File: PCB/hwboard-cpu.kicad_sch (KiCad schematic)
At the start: 2 parts, among them M1 CM0

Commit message: add sensors
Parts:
- removed JP1: ~{RPI_BOOT}, symbol Jumper:Jumper_2_Open
- removed M1: CM0, hwboard-bike-computer:CM0, symbol hwboard-bike-computer:CM0
- added U5: RASPBERRY_PI_ZERO_2_W, hwboard-bike-computer:MODULE_RASPBERRY_PI_ZERO_2_W, symbol hwboard-bike-computer:RASPBERRY_PI_ZERO_2_W
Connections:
- net 3V3_{OUT}: now also U5.1 (3V3_1), U5.17 (3V3_17)
- net 5V_{IN}: now also U5.2 (5V_2), U5.4 (5V_4)
- net GND: now also U5.14 (GND_14), U5.20 (GND_20), U5.25 (GND_25), U5.30 (GND_30), U5.34 (GND_34), U5.39 (GND_39), U5.6 (GND_6), U5.9 (GND_9)
- net I2C_{BUS}.SCL: now also U5.5 (GPIO3/SCL)
- net I2C_{BUS}.SDA: now also U5.3 (GPIO2/SDA1)
- new net SPI_{BUS}.MISO: U5.21 (GPIO9/SPI_MISO)
- new net SPI_{BUS}.MOSI: U5.19 (GPIO10/SPI_MOSI)
- new net SPI_{BUS}.SCLK: U5.23 (GPIO11/SPI_SCLK)
- new net SPI_{BUS}.~{CS}: U5.24 (GPIO8/SPI_~{CE0})
- new net UART_{BUS}.RX: U5.10 (GPIO15/RXD0)
- new net UART_{BUS}.TX: U5.8 (GPIO14/TXD0)
- no-connect marks 34 -> 0
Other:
- note added: "PinHeader 2x20 = 61304021121"

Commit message: Major change CPU and usage
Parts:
- removed U5: RASPBERRY_PI_ZERO_2_W, hwboard-bike-computer:MODULE_RASPBERRY_PI_ZERO_2_W, symbol hwboard-bike-computer:RASPBERRY_PI_ZERO_2_W
- added U5: STM32H743VITx, Package_QFP:LQFP-100_14x14mm_P0.5mm, symbol MCU_ST_STM32H7:STM32H743VITx
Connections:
- new net: U5.10 (VSS), U5.26 (VSS), U5.49 (VSS), U5.74 (VSS), U5.99 (VSS)
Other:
- note removed: "PinHeader 2x20 = 61304021121"

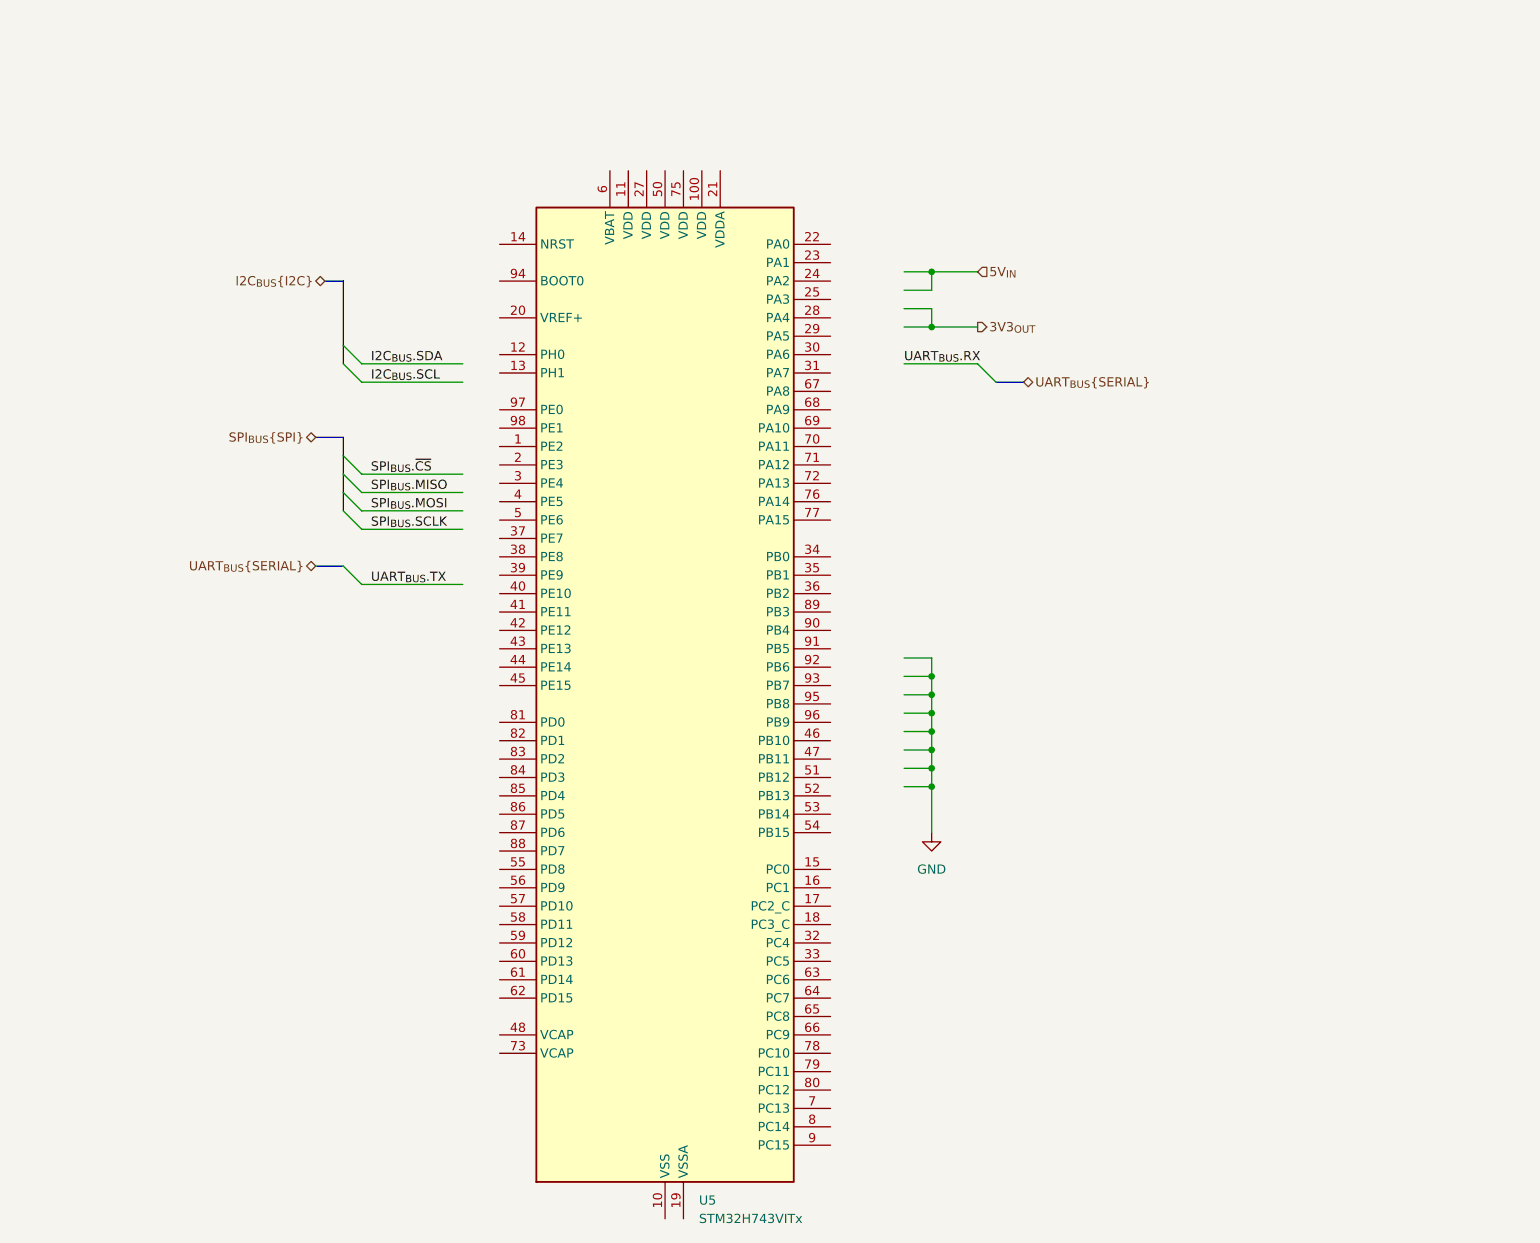
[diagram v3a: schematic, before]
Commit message: change of MCU and pins choosing
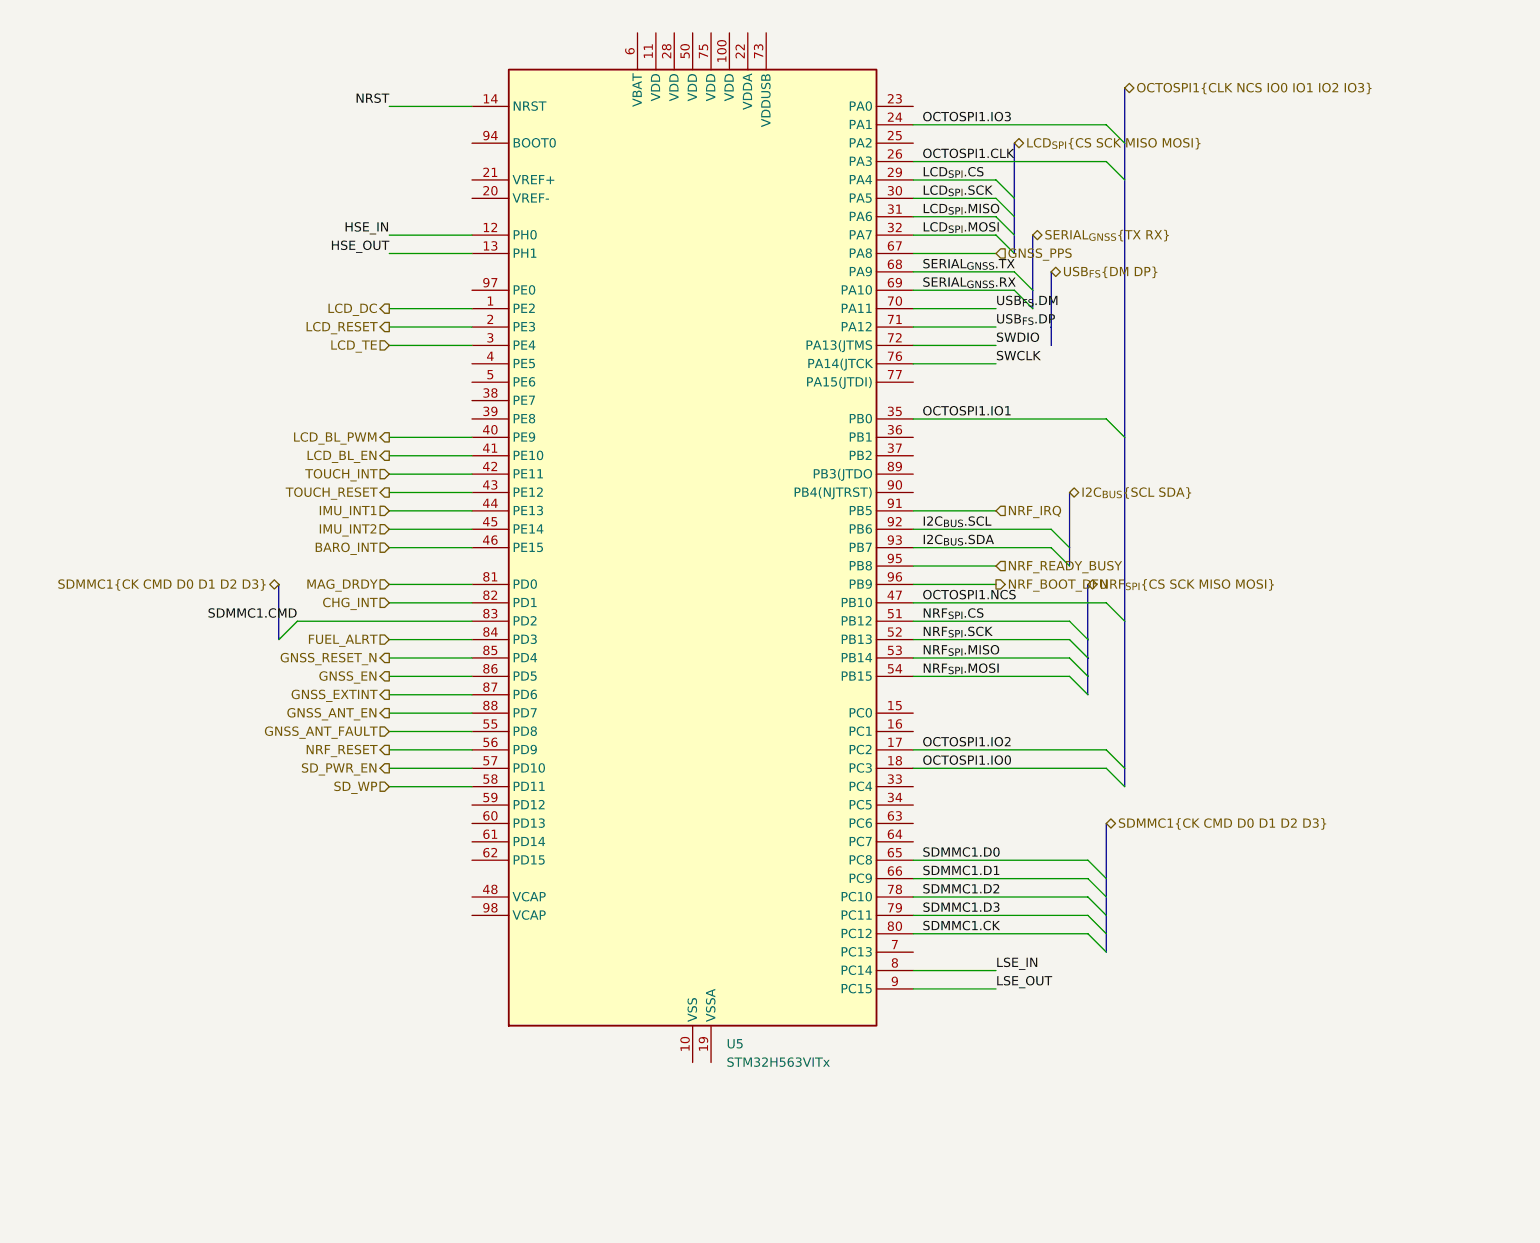
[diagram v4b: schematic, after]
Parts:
- removed U5: STM32H743VITx, Package_QFP:LQFP-100_14x14mm_P0.5mm, symbol MCU_ST_STM32H7:STM32H743VITx
- added U5: STM32H563VITx, Package_QFP:LQFP-100_14x14mm_P0.5mm, symbol MCU_ST_STM32H5:STM32H563VITx
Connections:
- net I2C_{BUS}.SCL: now also U5.92 (PB6)
- net I2C_{BUS}.SDA: now also U5.93 (PB7)
- new net: U5.10 (VSS), U5.27 (VSS), U5.49 (VSS), U5.74 (VSS), U5.99 (VSS)
- new net BARO_INT: U5.46 (PE15)
- new net CHG_INT: U5.82 (PD1)
- new net FUEL_ALRT: U5.84 (PD3)
- new net GNSS_ANT_EN: U5.88 (PD7)
- new net GNSS_ANT_FAULT: U5.55 (PD8)
- new net GNSS_EN: U5.86 (PD5)
- new net GNSS_EXTINT: U5.87 (PD6)
- new net GNSS_PPS: U5.67 (PA8)
- new net GNSS_RESET_N: U5.85 (PD4)
- new net HSE_IN: U5.12 (PH0)
- new net HSE_OUT: U5.13 (PH1)
- new net IMU_INT1: U5.44 (PE13)
- new net IMU_INT2: U5.45 (PE14)
- new net LCD_BL_EN: U5.41 (PE10)
- new net LCD_BL_PWM: U5.40 (PE9)
- new net LCD_DC: U5.1 (PE2)
- new net LCD_RESET: U5.2 (PE3)
- new net LCD_TE: U5.3 (PE4)
- new net LCD_{SPI}.CS: U5.29 (PA4)
- new net LCD_{SPI}.MISO: U5.31 (PA6)
- new net LCD_{SPI}.MOSI: U5.32 (PA7)
- new net LCD_{SPI}.SCK: U5.30 (PA5)
- new net LSE_IN: U5.8 (PC14)
- new net LSE_OUT: U5.9 (PC15)
- new net MAG_DRDY: U5.81 (PD0)
- new net NRF_BOOT_DFU: U5.96 (PB9)
- new net NRF_IRQ: U5.91 (PB5)
- new net NRF_READY_BUSY: U5.95 (PB8)
- new net NRF_RESET: U5.56 (PD9)
- new net NRF_{SPI}.CS: U5.51 (PB12)
- new net NRF_{SPI}.MISO: U5.53 (PB14)
- new net NRF_{SPI}.MOSI: U5.54 (PB15)
- new net NRF_{SPI}.SCK: U5.52 (PB13)
- new net NRST: U5.14 (NRST)
- new net OCTOSPI1.CLK: U5.26 (PA3)
- new net OCTOSPI1.IO0: U5.18 (PC3)
- new net OCTOSPI1.IO1: U5.35 (PB0)
- new net OCTOSPI1.IO2: U5.17 (PC2)
- new net OCTOSPI1.IO3: U5.24 (PA1)
- new net OCTOSPI1.NCS: U5.47 (PB10)
- new net SDMMC1.CK: U5.80 (PC12)
- new net SDMMC1.CMD: U5.83 (PD2)
- new net SDMMC1.D0: U5.65 (PC8)
- new net SDMMC1.D1: U5.66 (PC9)
- new net SDMMC1.D2: U5.78 (PC10)
- new net SDMMC1.D3: U5.79 (PC11)
- new net SD_PWR_EN: U5.57 (PD10)
- new net SD_WP: U5.58 (PD11)
- new net SERIAL_{GNSS}.RX: U5.69 (PA10)
- new net SERIAL_{GNSS}.TX: U5.68 (PA9)
- new net SWCLK: U5.76 (PA14(JTCK)
- new net SWDIO: U5.72 (PA13(JTMS)
- new net TOUCH_INT: U5.42 (PE11)
- new net TOUCH_RESET: U5.43 (PE12)
- new net USB_{FS}.DM: U5.70 (PA11)
- new net USB_{FS}.DP: U5.71 (PA12)
